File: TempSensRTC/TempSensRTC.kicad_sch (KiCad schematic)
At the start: 10 parts, among them J1 Pin Header 02x05, J2 DG308-2.54-02P-14-00AH, U1 MAX31865ATP_T, U2 MAX31855KASA_

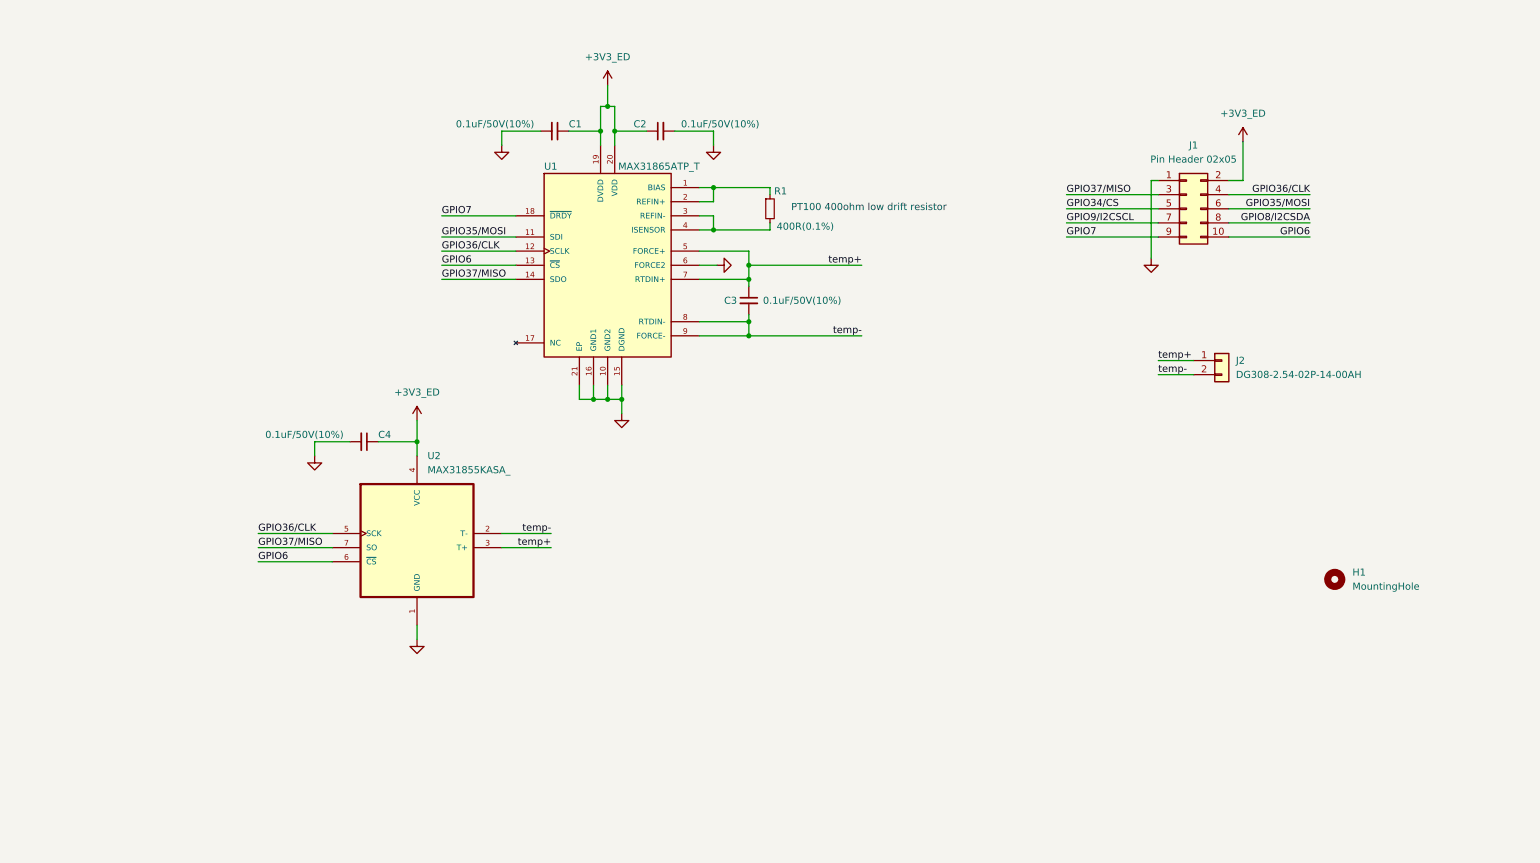
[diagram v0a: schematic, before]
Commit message: Structure changes to schematic files
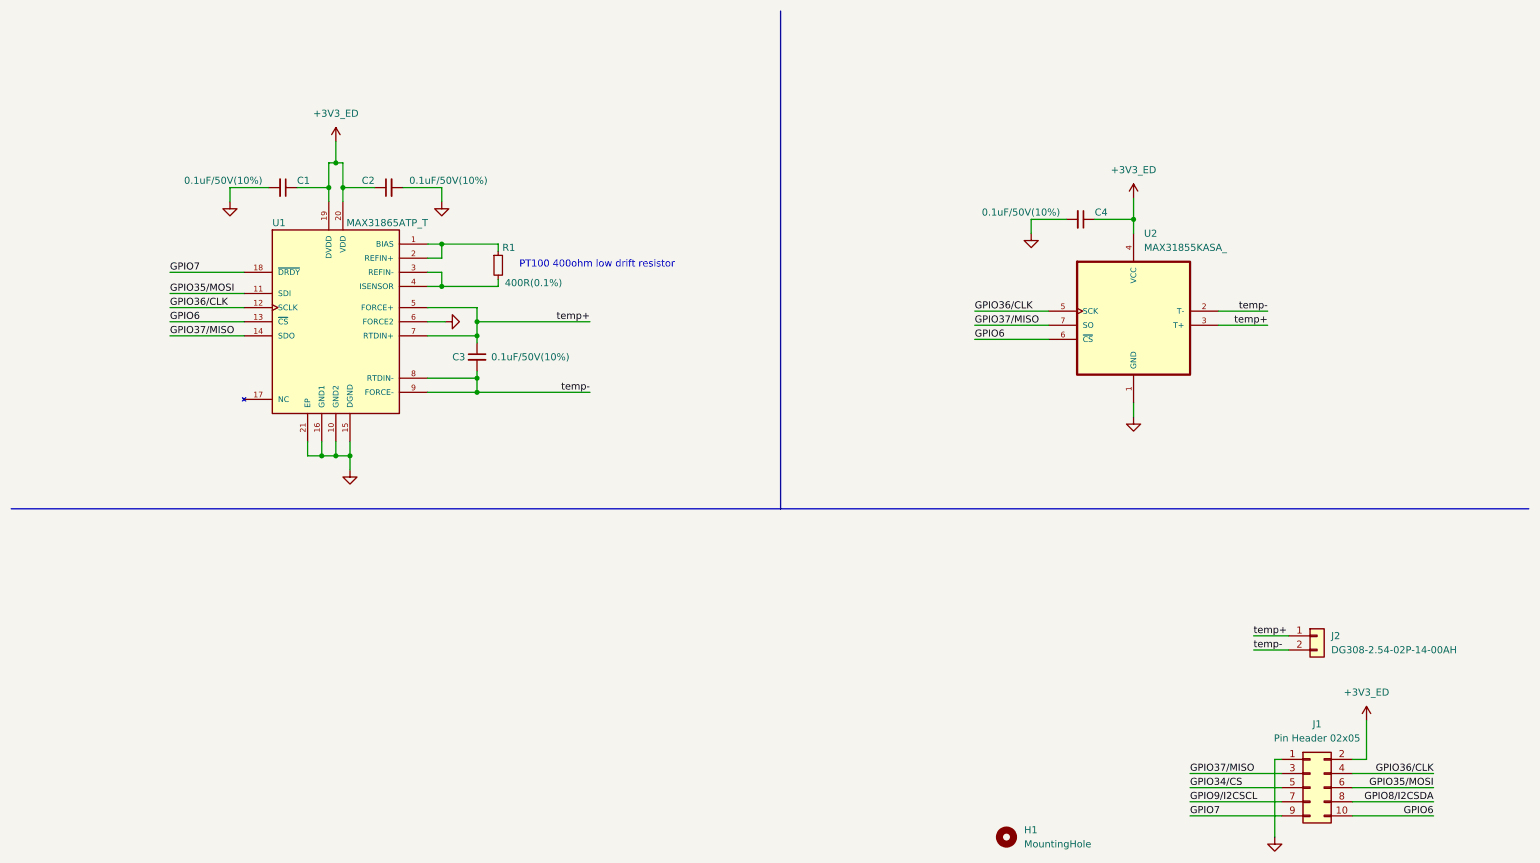
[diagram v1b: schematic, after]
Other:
- moved on the sheet: C1, C2, C3, C4, H1, J1, J2, R1, U1, U2
